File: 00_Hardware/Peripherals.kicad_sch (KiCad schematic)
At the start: 14 parts, among them J1 Conn_01x04_Pin, J3 Conn_01x04_Pin, J6 Conn_01x04_Pin, U6 FT231XS

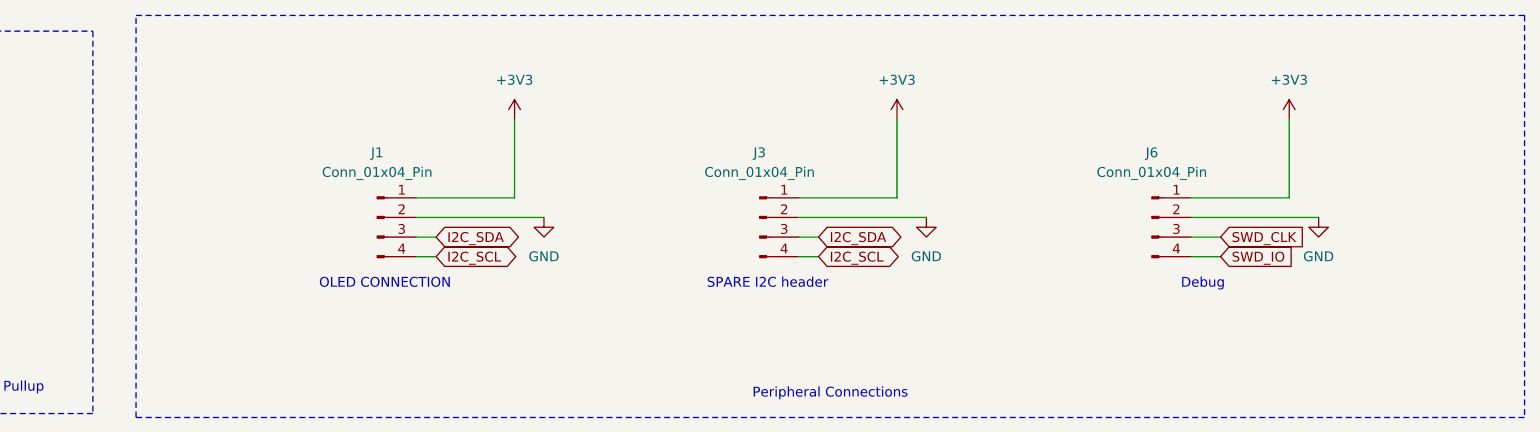
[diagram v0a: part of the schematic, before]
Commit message: Removed SMA for GPIO header placement.
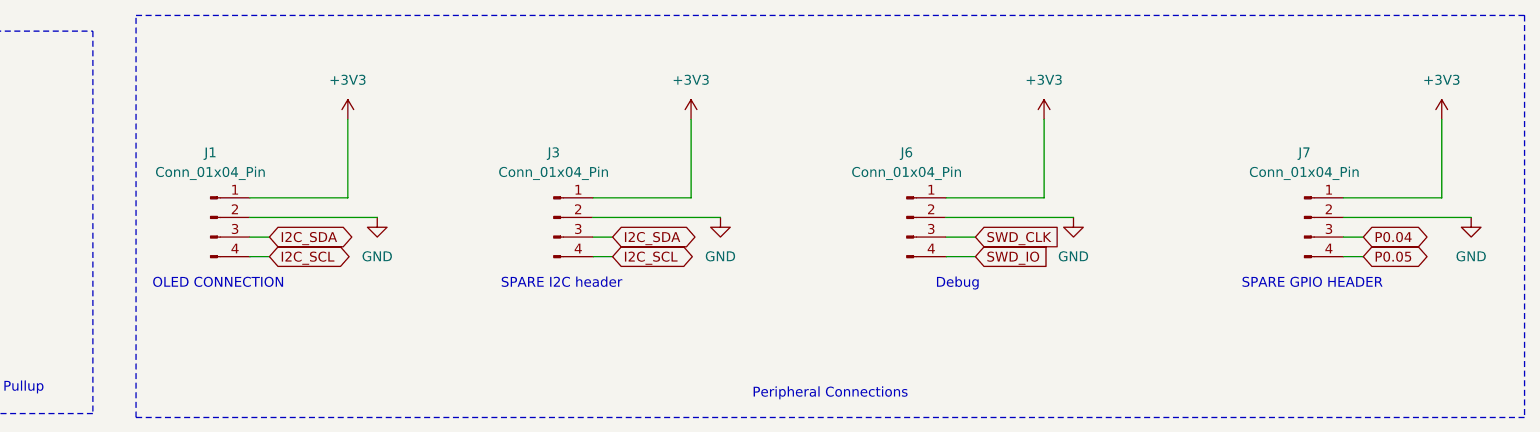
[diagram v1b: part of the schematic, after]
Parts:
- added J7: Conn_01x04_Pin, Connector_PinHeader_2.54mm:PinHeader_1x04_P2.54mm_Vertical, symbol Library:Conn_01x04_Pin
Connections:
- net +3V3: now also J7.1 (Pin_1)
- net GND: now also J7.2 (Pin_2)
- new net P0.04: J7.3 (Pin_3)
- new net P0.05: J7.4 (Pin_4)
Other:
- note added: "SPARE GPIO HEADER"
- moved on the sheet: J1, J3, J6

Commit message: updated from generated script
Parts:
- R18: value 10K -> 10k; LCSC (none) -> C25197
- R7, R8: value 270R_0603 -> 270R
